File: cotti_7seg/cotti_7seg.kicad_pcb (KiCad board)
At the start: 2 copper layers, 50.8 x 20.3 mm, 40 parts, among them J1 Pmod GPIO 2x06 pin, Q1 RE1C001UNTCL, Q10 RE1C001UNTCL, Q11 RE1C001UNTCL, Q12 RE1C001UNTCL, Q13 RE1C001UNTCL, Q14 RE1C001UNTCL, Q15 RE1C001UNTCL, Q16 RE1C001UNTCL, Q2 RE1C001UNTCL, Q3 RE1C001UNTCL, Q4 RE1C001UNTCL, Q5 RE1C001UNTCL, Q6 RE1C001UNTCL, Q7 RE1C001UNTCL, Q8 RE1C001UNTCL, Q9 RE1C001UNTCL, U1 BCD_to_7seg, U2 157119S12701, U3 SN74LVC1G08DBVR-EV, U4 BCD_to_7seg, U5 157119S12701, U6 SN74LVC1G08DBVR-EV

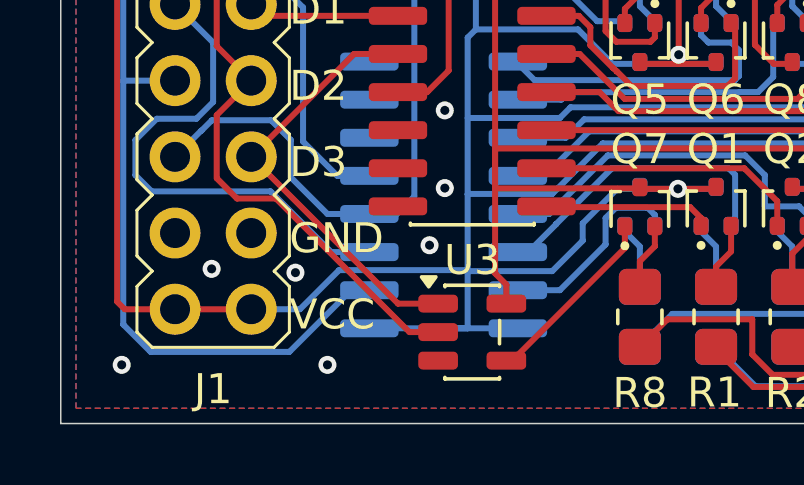
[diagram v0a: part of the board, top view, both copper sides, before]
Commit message: fix: change "vcc" to "3v3" power input
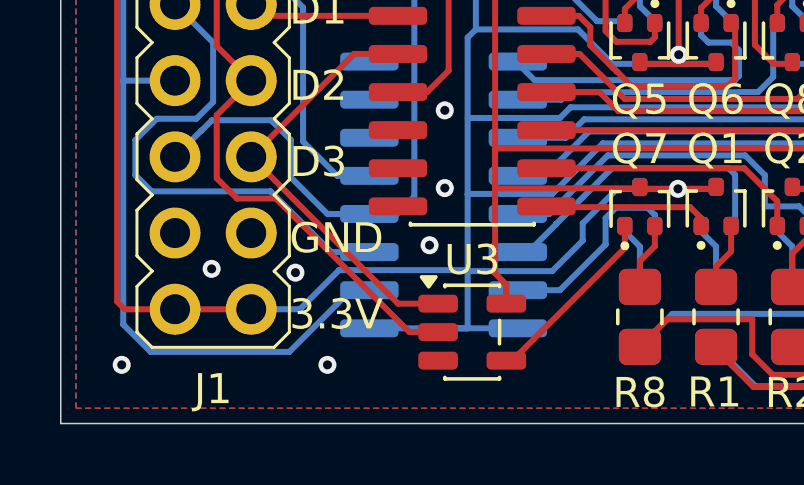
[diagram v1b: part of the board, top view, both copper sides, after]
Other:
- board text added: "3.3V"
- board text removed: "VCC"
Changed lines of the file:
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@@
 		)
 	)
-	(gr_text "VCC"
+	(gr_text "3.3V"
 		(at 109.22 68.072 0)
 		(layer "F.SilkS")
